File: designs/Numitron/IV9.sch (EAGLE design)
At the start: 13 parts, among them IC1 TLC5916IN, IC2 TLC5916IN, IC3 TLC5916IN, IC4 TLC5916IN

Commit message: added numitrons for tube clock
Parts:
- removed SV1: (no value), con-lstb:MA08-1
- removed TUBE1, TUBE2, TUBE3, TUBE4: (no value), NixieTube:DA-2000
- added 1, 2, 3, 4: IV-9, domestichacks:IV-9
- added SV2: (no value), CommonParts:PINHEADER-1X8
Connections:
- removed net N$1: IC3.!OUT3, IC4.!OUT3, TUBE3.G, TUBE4.G
- removed net N$10: IC1.!OUT5, TUBE1.B
- removed net N$11: IC1.!OUT6, TUBE1.F
- removed net N$12: IC2.!OUT0, TUBE2.E
- removed net N$14: IC2.!OUT1, TUBE2.D
- removed net N$2: IC3.!OUT4, IC4.!OUT4, TUBE3.A, TUBE4.A
- removed net N$3: IC1.!OUT0, TUBE1.E
- removed net N$33: IC2.!OUT2, TUBE2.C
- removed net N$34: IC2.!OUT3, TUBE2.G
- removed net N$37: IC2.!OUT4, TUBE2.A
- removed net N$38: IC2.!OUT5, TUBE2.B
- removed net N$39: IC2.!OUT6, TUBE2.F
- removed net N$4: IC1.!OUT1, TUBE1.D
- removed net N$40: IC3.!OUT0, TUBE3.E
- removed net N$41: IC3.!OUT1, TUBE3.D
- removed net N$42: IC3.!OUT2, TUBE3.C
- removed net N$43: IC4.!OUT0, TUBE4.E
- removed net N$44: IC4.!OUT1, TUBE4.D
- removed net N$45: IC3.!OUT5, TUBE3.B
- removed net N$46: IC3.!OUT6, TUBE3.F
- removed net N$47: IC4.!OUT2, TUBE4.C
- removed net N$5: IC1.!OUT2, TUBE1.C
- removed net N$50: IC4.!OUT5, TUBE4.B
- removed net N$51: IC4.!OUT6, TUBE4.F
- removed net N$6: IC1.!OUT3, TUBE1.G
- removed net N$8: IC1.!OUT4, TUBE1.A
- new net A_1: 1.5, IC1.!OUT4
- new net A_2: 2.5, IC2.!OUT4
- new net A_3: 3.5, IC3.!OUT4
- new net A_4: 4.5, IC4.!OUT4
- new net B_1: 1.3, IC1.!OUT5
- new net B_2: 2.3, IC2.!OUT5
- new net B_3: 3.3, IC3.!OUT5
- new net B_4: 4.3, IC4.!OUT5
- new net C_1: 1.4, IC1.!OUT2
- new net C_2: 2.4, IC2.!OUT2
- new net C_3: 3.4, IC3.!OUT2
- new net C_4: 4.4, IC4.!OUT2
- new net DEC_1: 1.2, IC1.!OUT7
- new net DEC_2: 2.2, IC2.!OUT7
- new net DEC_3: 3.2, IC3.!OUT7
- new net DEC_4: 4.2, IC4.SDO
- new net D_1: 1.8, IC1.!OUT1
- new net D_2: 2.8, IC2.!OUT1
- new net D_3: 3.8, IC3.!OUT1
- new net D_4: 4.8, IC4.!OUT1
- new net E_1: 1.9, IC1.!OUT0
- new net E_2: 2.9, IC2.!OUT0
- new net E_3: 3.9, IC3.!OUT0
- new net E_4: 4.9, IC4.!OUT0
- new net F_1: 1.6, IC1.!OUT6
- new net F_2: 2.6, IC2.!OUT6
- new net F_3: 3.6, IC3.!OUT6
- new net F_4: 4.6, IC4.!OUT6
- new net G_1: 1.7, IC1.!OUT3
- new net G_2: 2.7, IC2.!OUT3
- new net G_3: 3.7, IC3.!OUT3
- new net G_4: 4.7, IC4.!OUT3
- net 3.3V: now also SV2.8; no longer SV1.8
- net DS: now also SV2.1; no longer SV1.1
- net GND: now also 1.1, 2.1, 3.1, 4.1, SV2.5, SV2.7; no longer SV1.5, SV1.7, TUBE1.COM, TUBE2.COM, TUBE3.COM, TUBE4.COM
- net NC: now also SV2.6; no longer SV1.6
- net NC2: now also SV2.4; no longer SV1.4
- net SH_CP: now also SV2.2; no longer SV1.2
- net ST_CP: now also SV2.3; no longer SV1.3

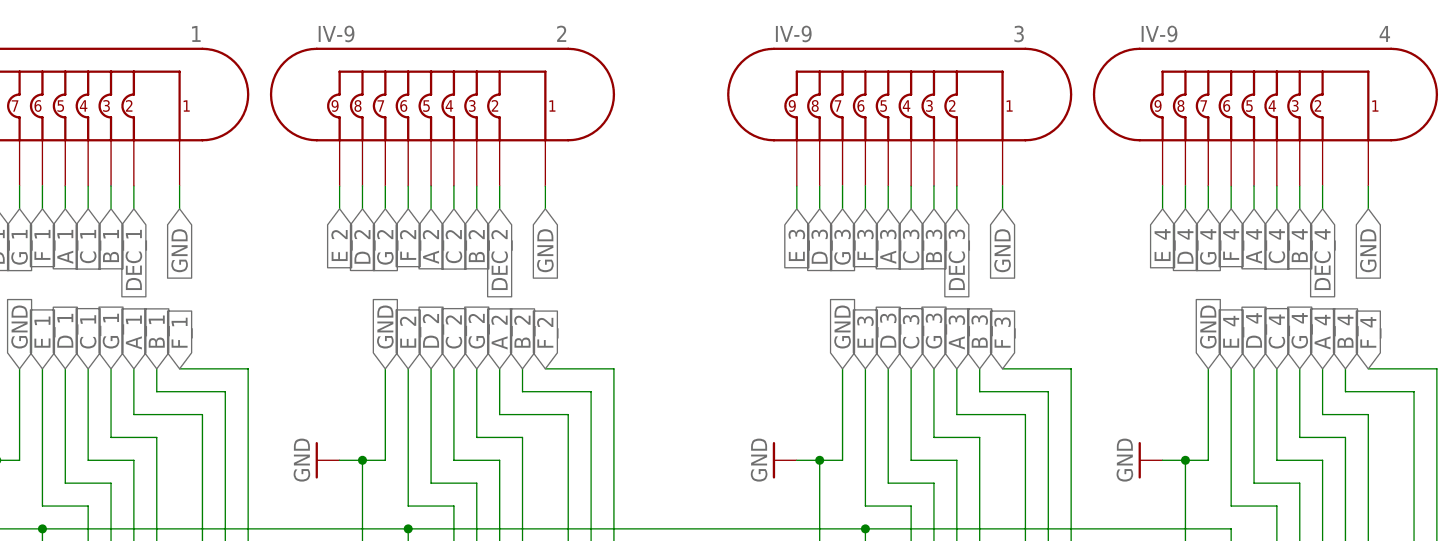
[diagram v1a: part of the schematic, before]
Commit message: changes for new design excluding swap for amplifier
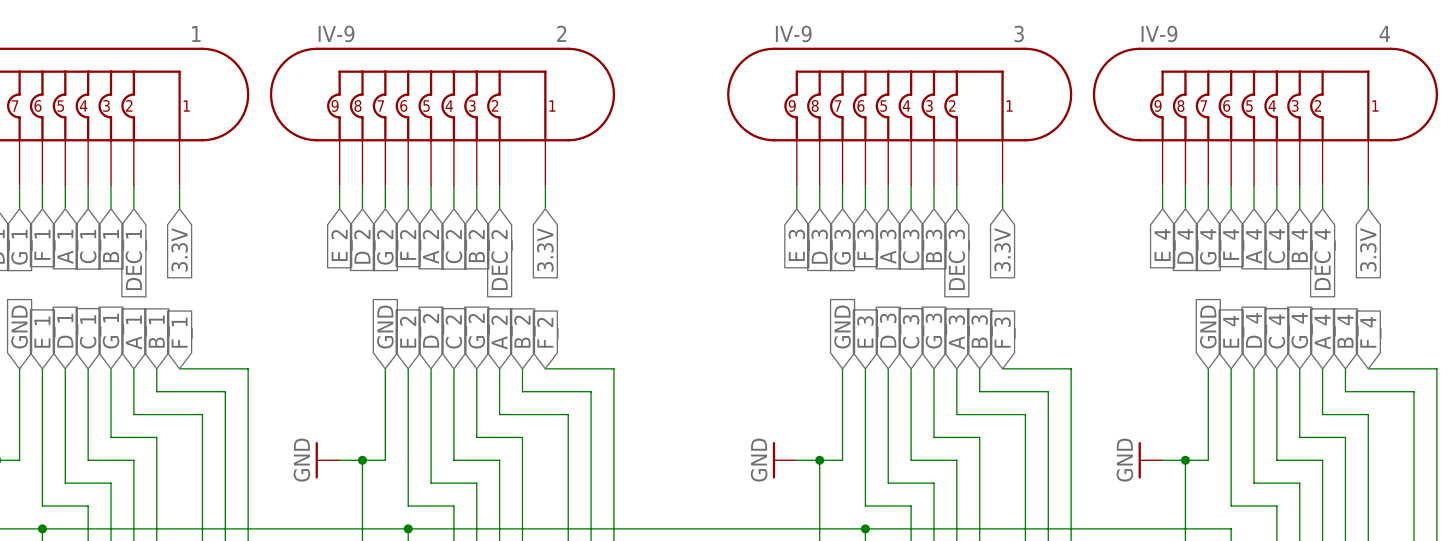
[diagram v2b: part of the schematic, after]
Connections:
- net 3.3V: now also 1.1, 2.1, 3.1, 4.1
- net GND: no longer 1.1, 2.1, 3.1, 4.1
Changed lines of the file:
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@@
 <?xml version="1.0" encoding="utf-8"?>
 <!DOCTYPE eagle SYSTEM "eagle.dtd">
-<eagle version="9.5.2">
+<eagle version="9.6.2">
 <drawing>
 <settings>
@@
 <pinref part="SV2" gate="1" pin="7"/>
 </segment>
-<segment>
-<pinref part="1" gate="T1" pin="1"/>
-<wire x1="63.5" y1="154.94" x2="63.5" y2="152.4" width="0.1524" layer="91"/>
-<label x="63.5" y="152.4" size="1.778" layer="95" rot="R270" xref="yes"/>
-</segment>
-<segment>
-<pinref part="2" gate="T1" pin="1"/>
-<wire x1="104.14" y1="154.94" x2="104.14" y2="152.4" width="0.1524" layer="91"/>
-<label x="104.14" y="152.4" size="1.778" layer="95" rot="R270" xref="yes"/>
-</segment>
-<segment>
-<pinref part="3" gate="T1" pin="1"/>
-<wire x1="154.94" y1="154.94" x2="154.94" y2="152.4" width="0.1524" layer="91"/>
-<label x="154.94" y="152.4" size="1.778" layer="95" rot="R270" xref="yes"/>
-</segment>
-<segment>
-<pinref part="4" gate="T1" pin="1"/>
-<wire x1="195.58" y1="154.94" x2="195.58" y2="152.4" width="0.1524" layer="91"/>
-<label x="195.58" y="152.4" size="1.778" layer="95" rot="R270" xref="yes"/>
-</segment>
 </net>
 <net name="3.3V" class="0">
@@
 <junction x="43.18" y="53.34"/>
 </segment>
+<segment>
+<pinref part="1" gate="T1" pin="1"/>
+<wire x1="63.5" y1="154.94" x2="63.5" y2="152.4" width="0.1524" layer="91"/>
+<label x="63.5" y="152.4" size="1.778" layer="95" rot="R270" xref="yes"/>
+</segment>
+<segment>
+<pinref part="2" gate="T1" pin="1"/>
+<wire x1="104.14" y1="154.94" x2="104.14" y2="152.4" width="0.1524" layer="91"/>
+<label x="104.14" y="152.4" size="1.778" layer="95" rot="R270" xref="yes"/>
+</segment>
+<segment>
+<pinref part="3" gate="T1" pin="1"/>
+<wire x1="154.94" y1="154.94" x2="154.94" y2="152.4" width="0.1524" layer="91"/>
+<label x="154.94" y="152.4" size="1.778" layer="95" rot="R270" xref="yes"/>
+</segment>
+<segment>
+<pinref part="4" gate="T1" pin="1"/>
+<wire x1="195.58" y1="154.94" x2="195.58" y2="152.4" width="0.1524" layer="91"/>
+<label x="195.58" y="152.4" size="1.778" layer="95" rot="R270" xref="yes"/>
+</segment>
 </net>
